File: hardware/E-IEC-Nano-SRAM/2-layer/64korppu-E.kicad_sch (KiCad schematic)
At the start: 23 parts, among them J1 IEC_DIN-6, J2 Floppy_34pin, J3 DC_5V, U1 Arduino_Nano, U2 23LC1024, U3 74HC595

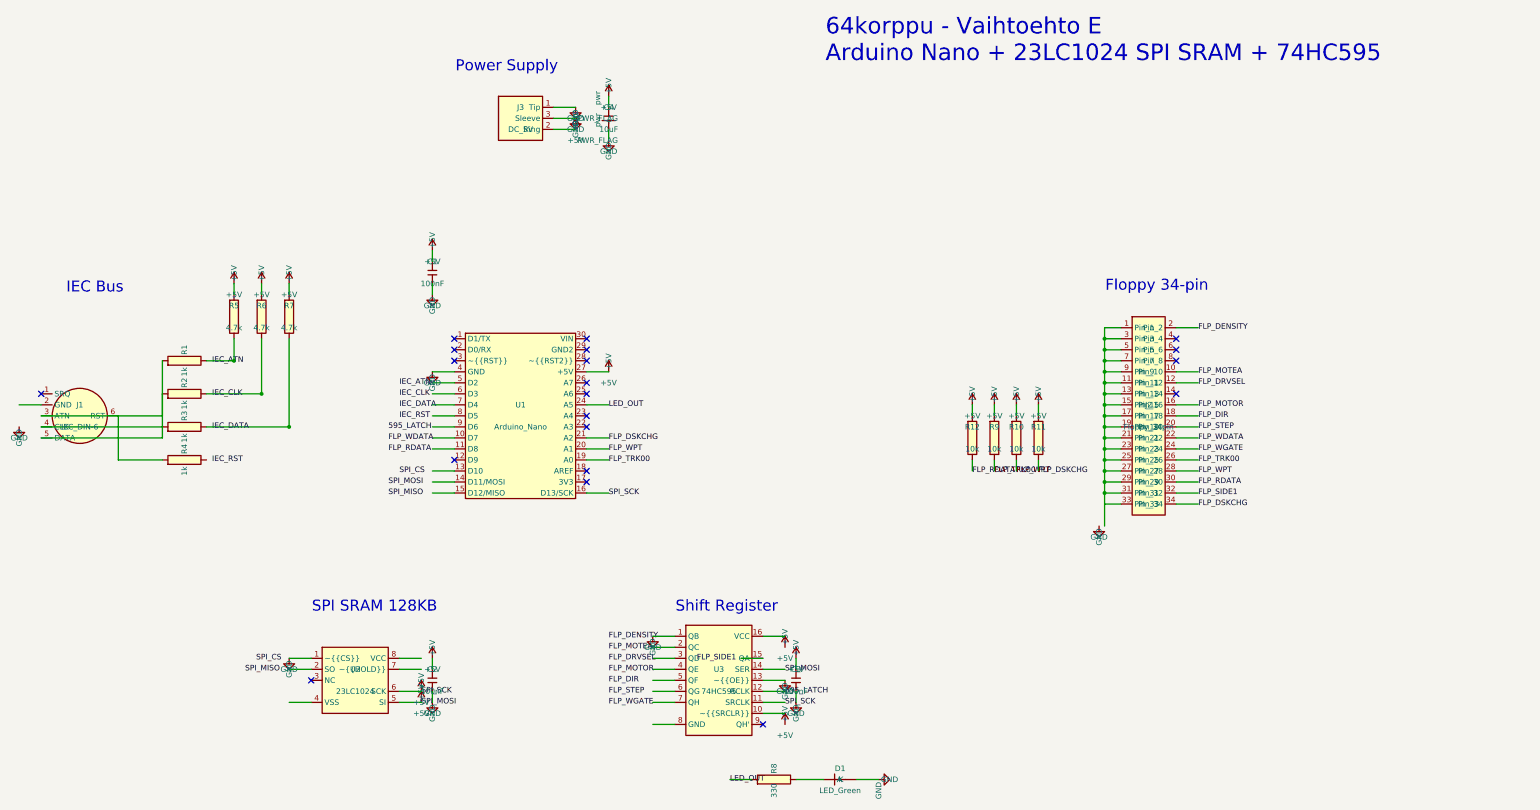
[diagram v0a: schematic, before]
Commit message: Switch SRAM from 23LC1024 (128KB) to 23LC256 (32KB), fix 74HC595 QA pin docs
- Replace 23LC1024 with 23LC256: same DIP-8 pinout, 16-bit addressing
- SRAM driver: 24-bit → 16-bit address (drop one spi_transfer call)
- SimAVR harness: update SRAM emulation to 2-byte addressing and 32KB
- Fix piirikaavio.md: QA was incorrectly marked as unused (is /SIDE1)
- Fix shiftreg.h bit mapping comment to match actual hardware wiring
- Update all docs, schematics, PCB files, tools for both 2-layer and 4-layer

Actual SRAM usage is ~22KB, so 32KB is sufficient with margin.

Co-Authored-By: Claude Opus 4.6 <noreply@anthropic.com>
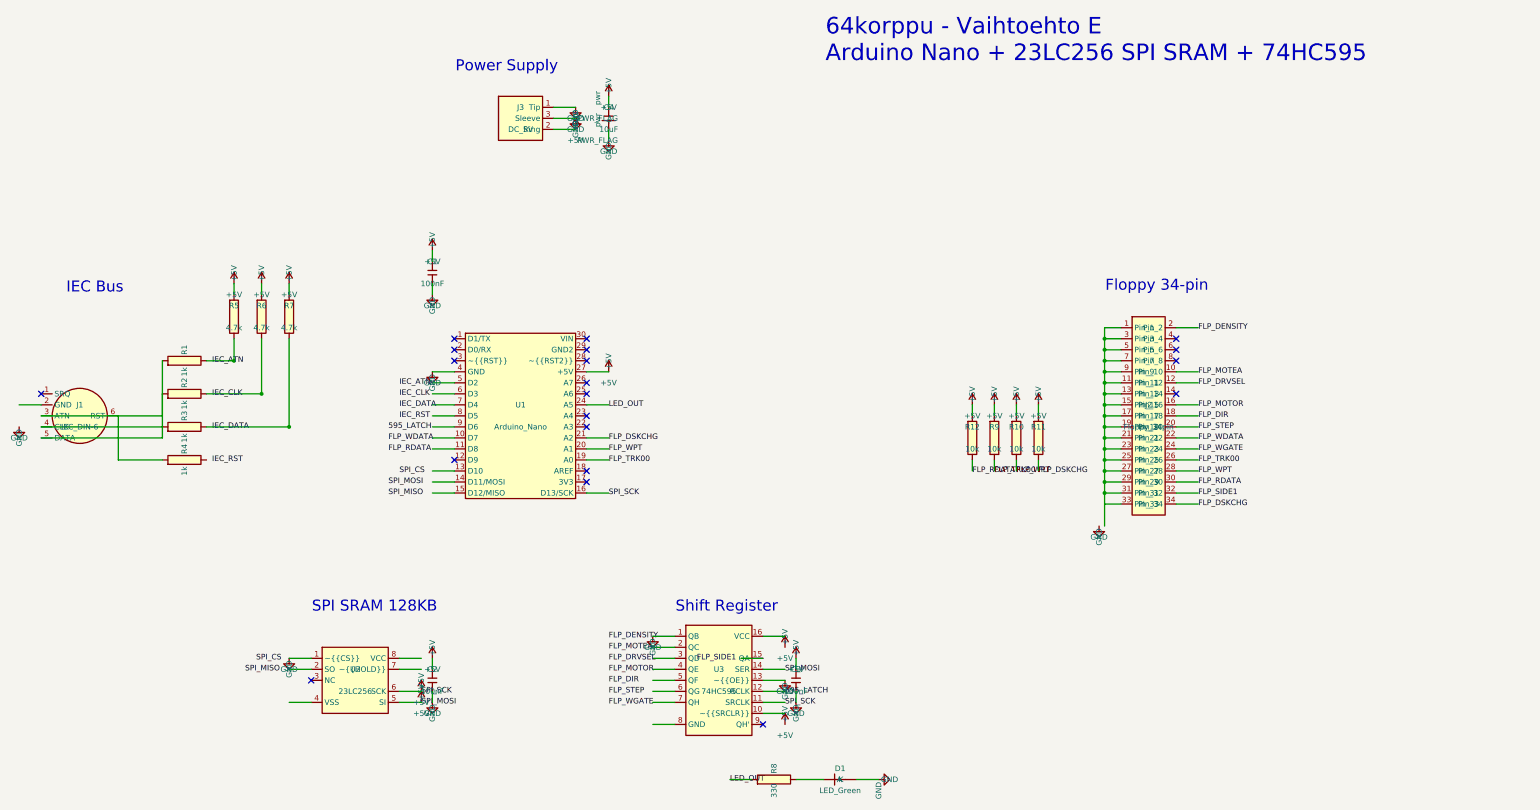
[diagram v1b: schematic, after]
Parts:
- U2: value 23LC1024 -> 23LC256; symbol 64korppu-E:23LC1024 -> 64korppu-E:23LC256
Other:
- note added: "64korppu - Vaihtoehto E Arduino Nano + 23LC256 SPI SRAM + 74HC595"
- note removed: "64korppu - Vaihtoehto E Arduino Nano + 23LC1024 SPI SRAM + 74HC595"
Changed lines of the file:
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@@
     )
   )
-  (symbol (lib_id "64korppu-E:23LC1024") (at 101.60 162.56 0)
+  (symbol (lib_id "64korppu-E:23LC256") (at 101.60 162.56 0)
     (property "Reference" "U2"
       (at 101.60 160.02 0)
       (effects (font (size 1.27 1.27)))
     )
-    (property "Value" "23LC1024"
+    (property "Value" "23LC256"
       (at 101.60 165.10 0)
       (effects (font (size 1.27 1.27)))
@@
   (no_connect (at 29.21 96.52)
   )
-  (text "64korppu - Vaihtoehto E\nArduino Nano + 23LC1024 SPI SRAM + 74HC595"
+  (text "64korppu - Vaihtoehto E\nArduino Nano + 23LC256 SPI SRAM + 74HC595"
     (at 210 15 0)
     (effects (font (size 3.81 3.81)) (justify left))

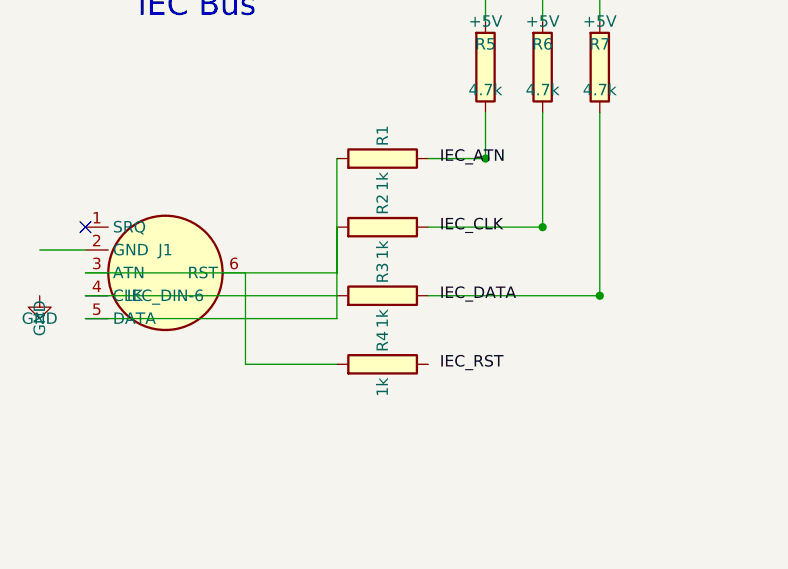
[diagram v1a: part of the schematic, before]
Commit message: Change IEC series resistors R1-R4 from 1kΩ to 100Ω
1kΩ was too large — formed a voltage divider with C64's pull-ups,
keeping the IEC bus at ~2.5V instead of LOW. 100Ω provides ESD
protection while allowing proper LOW signaling (~0.45V).

Updated schematics (2-layer + 4-layer) and all documentation.

Co-Authored-By: Claude Opus 4.6 (1M context) <noreply@anthropic.com>
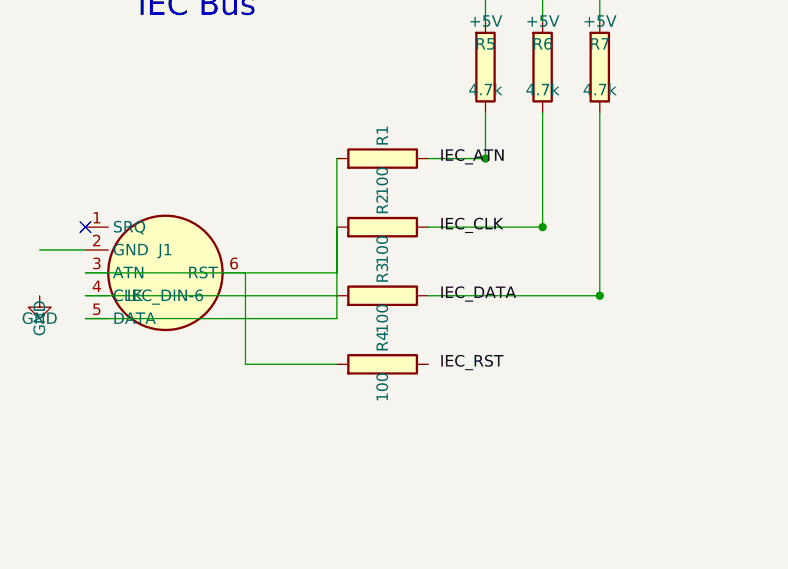
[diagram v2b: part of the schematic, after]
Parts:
- R1, R2, R3, R4: value 1k -> 100
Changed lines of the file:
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@@
       (effects (font (size 1.27 1.27)))
     )
-    (property "Value" "1k"
+    (property "Value" "100"
       (at 62.23 91.44 0)
       (effects (font (size 1.27 1.27)))
@@
       (effects (font (size 1.27 1.27)))
     )
-    (property "Value" "1k"
+    (property "Value" "100"
       (at 62.23 99.06 0)
       (effects (font (size 1.27 1.27)))
@@
       (effects (font (size 1.27 1.27)))
     )
-    (property "Value" "1k"
+    (property "Value" "100"
       (at 62.23 106.68 0)
       (effects (font (size 1.27 1.27)))
@@
       (effects (font (size 1.27 1.27)))
     )
-    (property "Value" "1k"
+    (property "Value" "100"
       (at 62.23 114.30 0)
       (effects (font (size 1.27 1.27)))
